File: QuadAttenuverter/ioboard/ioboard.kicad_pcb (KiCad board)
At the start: 2 copper layers, 35.6 x 108 mm, 38 parts, among them J1 Conn_01x09, J2 Conn_02x10_Counter_Clockwise

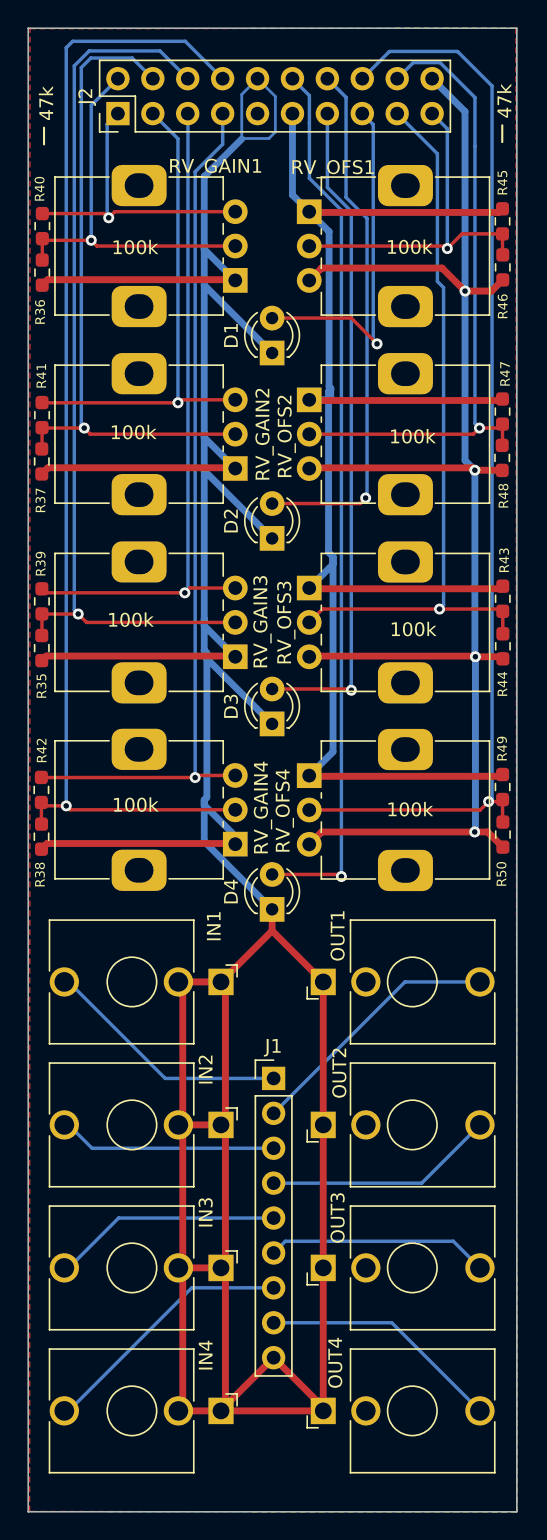
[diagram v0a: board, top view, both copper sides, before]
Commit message: Add M3 mount for mechanical stability, and update power
If pots are used that don't have mounting brackets, the faceplate needs
extra mechanical support at the top. Two M3 screws can support that.

In addition, bottom silk screen is added for the power connector, since
it's probably going to be mounted there.
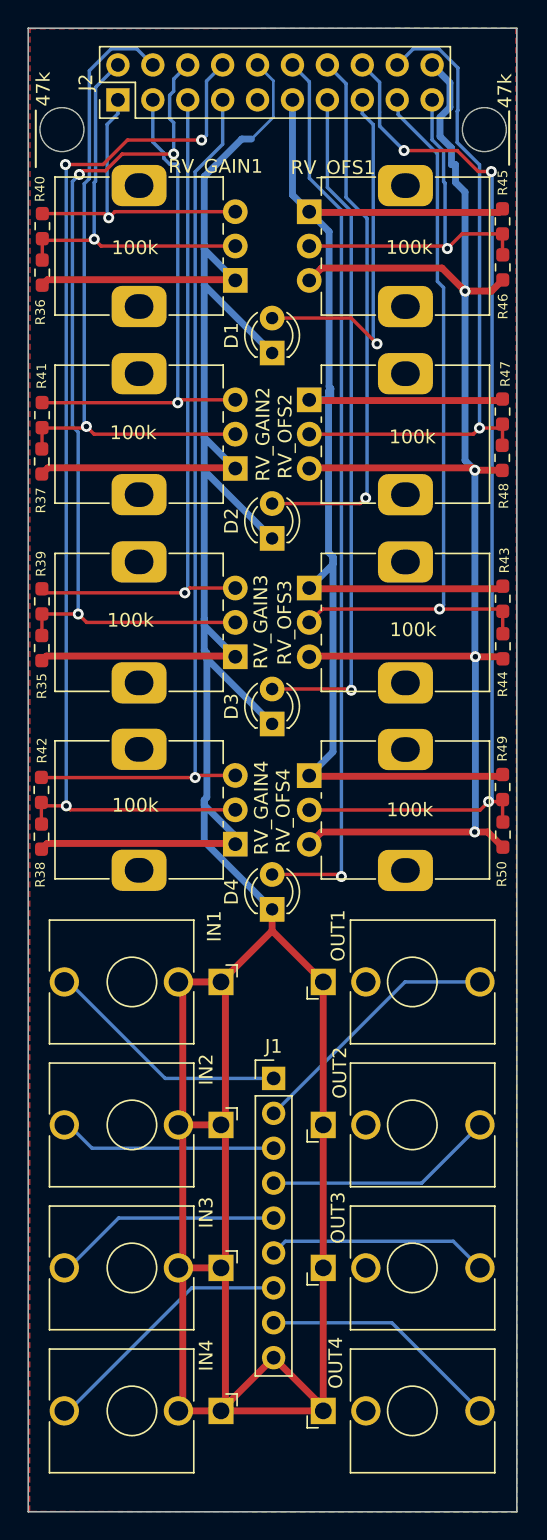
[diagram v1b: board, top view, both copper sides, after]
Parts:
- added REF**: MountingHole_3.2mm_M3_NoCourt, Library:MountingHole_3.2mm_M3_NoCourt, F.Cu at (85.6, 46.7)
- added REF**: MountingHole_3.2mm_M3_NoCourt, Library:MountingHole_3.2mm_M3_NoCourt, F.Cu at (116.3, 46.7)
- moved J2 1.00 mm to (89.7, 44.6)
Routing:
- net GND: track 300.8 -> 296.1 mm
- net /GAIN4OUT: track 83.8 -> 79.3 mm, vias 1 -> 3
- net /OFFSET4: track 79.5 -> 76.5 mm, vias 1 -> 3
- net /GAIN3OUT: track 65.4 -> 62.9 mm, vias 1 -> 3
- net -5V: track 114.9 -> 116.9 mm
- net /GAIN2IN: track 36.0 -> 37.3 mm
- net /GAIN3IN: track 49.3 -> 50.6 mm
- net /OFFSET3: track 53.8 -> 54.8 mm
- net /OFFSET1: track 26.4 -> 27.4 mm
- net /LED4: track 64.6 -> 65.6 mm
- net /LED3: track 48.5 -> 49.5 mm
- net /LED2: track 38.7 -> 39.7 mm
- net /LED1: track 25.6 -> 26.6 mm
- net /GAIN4IN: track 63.3 -> 64.3 mm
- net /GAIN1IN: track 22.3 -> 23.3 mm
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
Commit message: Fix the pinout of the offset POTs so right is plus
These were reversed (it's an inverting amplifier) in the original
design. Also added a marking to the board.
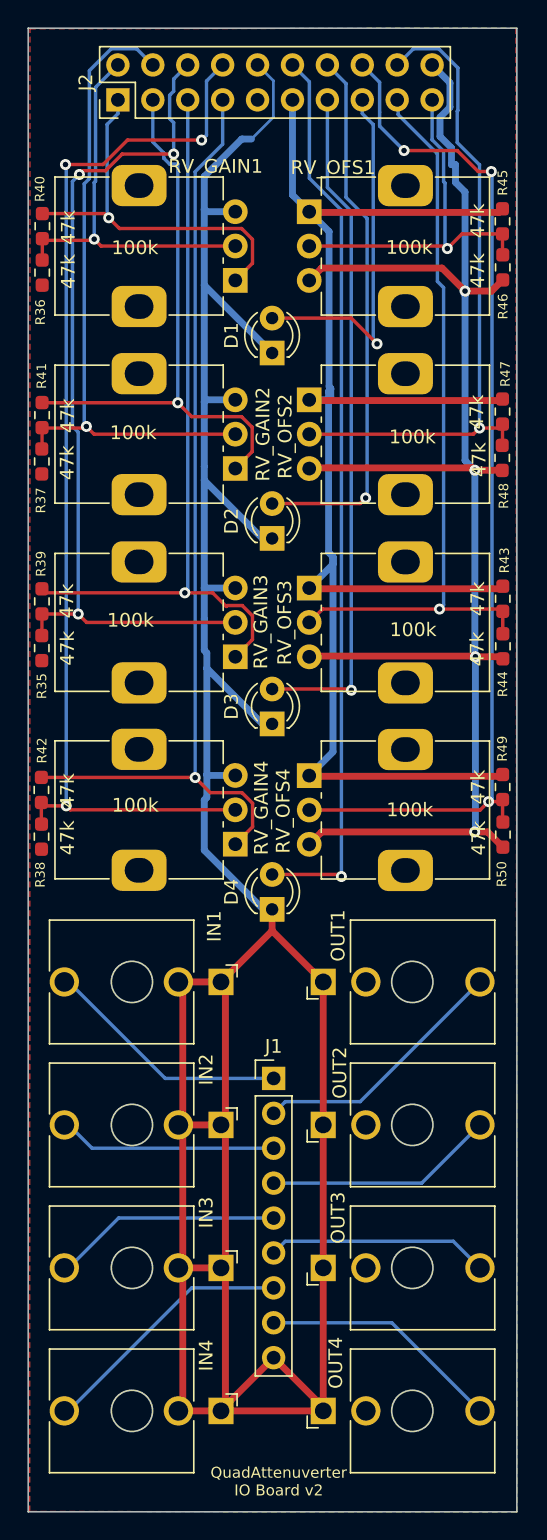
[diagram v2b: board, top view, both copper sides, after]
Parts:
- removed REF** (x2): MountingHole_3.2mm_M3_NoCourt, Library:MountingHole_3.2mm_M3_NoCourt
- D1, D2, D3, D4: footprint Library:LED_D3.0mm_Himount -> LED_THT:LED_D3.0mm
- IN1, IN2, IN3, IN4, OUT1, OUT2, OUT3, OUT4: footprint Connector_Audio:Jack_3.5mm_QingPu_WQP-PJ398SM_Vertical_CircularHoles -> Library:Jack_3.5mm_QingPu_WQP-PJ398SM_Vertical_CircularHoles_Hole
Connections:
- RV_GAIN1 pad 1: GND -> /GAIN1IN
- RV_GAIN1 pad 3: /GAIN1IN -> GND
- RV_GAIN2 pad 1: GND -> /GAIN2IN
- RV_GAIN2 pad 3: /GAIN2IN -> GND
- RV_GAIN3 pad 1: GND -> /GAIN3IN
- RV_GAIN3 pad 3: /GAIN3IN -> GND
- RV_GAIN4 pad 1: GND -> /GAIN4IN
- RV_GAIN4 pad 3: /GAIN4IN -> GND
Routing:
- net GND: track 296.1 -> 232.0 mm
- net /GAIN4IN: track 64.3 -> 69.8 mm
- net /GAIN2IN: track 37.3 -> 42.7 mm
- net /GAIN3IN: track 50.6 -> 56.0 mm
- net /GAIN1IN: track 23.3 -> 28.5 mm
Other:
- board text added: "QuadAttenuverter IO Board v2"
- board text removed: "47k"
